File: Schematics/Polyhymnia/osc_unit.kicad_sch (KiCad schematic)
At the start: 7 parts, among them J4 Conn_02x05_Counter_Clockwise, SW10 RotaryEncoder, SW5 RotaryEncoder

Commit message: Added schematics for OSC, Filter and Envelope and updated README
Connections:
- no-connect marks 0 -> 1
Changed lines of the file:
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@@
 		(color 0 0 0 0)
 	)
+	(no_connect
+		(at 157.48 59.69)
+	)
 	(wire
 		(pts
@@
 		(pts
 			(xy 132.08 64.77) (xy 144.78 64.77)
+		)
+		(stroke
+			(width 0)
+			(type default)
+		)
+	)
+	(wire
+		(pts
+			(xy 5.4074 0.8096) (xy 5.4074 5.8896)
 		)
 		(stroke
@@
 			)
 			(justify left)
+		)
+	)
+	(hierarchical_label "GND"
+		(shape input)
+		(at 5.4074 0.8096 180)
+		(effects
+			(font
+				(size 1.27 1.27)
+			)
+			(justify right)
 		)
 	)
@@
 		(instances
 			(project "Polyhymnia"
-				(path "/e4936a91-9e28-4906-9468-02ad94b9239b/04017fce-ab7a-4c45-a3b8-5493e5fdc4a7"
+				(path "/e4936a91-9e28-4906-9468-02ad94b9239b/3627614c-7dfe-4a8f-9547-cf9b2f9e6ef0/0d039393-a65a-4236-aaaa-38dedb739ff5"
+					(reference "SW12")
+					(unit 1)
+				)
+				(path "/e4936a91-9e28-4906-9468-02ad94b9239b/3627614c-7dfe-4a8f-9547-cf9b2f9e6ef0/89248004-8614-47a4-bd14-f15ba37dba97"
+					(reference "SW14")
+					(unit 1)
+				)
+				(path "/e4936a91-9e28-4906-9468-02ad94b9239b/3627614c-7dfe-4a8f-9547-cf9b2f9e6ef0/a5d4020b-3f52-4bac-b91d-f4cfb91e59d1"
 					(reference "SW5")
-					(unit 1)
-				)
-				(path "/e4936a91-9e28-4906-9468-02ad94b9239b/4ef4e00a-50a0-4639-950e-6d0b1ade7b2c"
-					(reference "SW14")
-					(unit 1)
-				)
-				(path "/e4936a91-9e28-4906-9468-02ad94b9239b/acb5abcb-989c-4dca-8a1a-ed3e163b2d20"
-					(reference "SW12")
 					(unit 1)
 				)
@@
 		(instances
 			(project "Polyhymnia"
-				(path "/e4936a91-9e28-4906-9468-02ad94b9239b/04017fce-ab7a-4c45-a3b8-5493e5fdc4a7"
+				(path "/e4936a91-9e28-4906-9468-02ad94b9239b/3627614c-7dfe-4a8f-9547-cf9b2f9e6ef0/0d039393-a65a-4236-aaaa-38dedb739ff5"
+					(reference "D38")
+					(unit 1)
+				)
+				(path "/e4936a91-9e28-4906-9468-02ad94b9239b/3627614c-7dfe-4a8f-9547-cf9b2f9e6ef0/89248004-8614-47a4-bd14-f15ba37dba97"
+					(reference "D42")
+					(unit 1)
+				)
+				(path "/e4936a91-9e28-4906-9468-02ad94b9239b/3627614c-7dfe-4a8f-9547-cf9b2f9e6ef0/a5d4020b-3f52-4bac-b91d-f4cfb91e59d1"
 					(reference "D35")
-					(unit 1)
-				)
-				(path "/e4936a91-9e28-4906-9468-02ad94b9239b/4ef4e00a-50a0-4639-950e-6d0b1ade7b2c"
-					(reference "D42")
-					(unit 1)
-				)
-				(path "/e4936a91-9e28-4906-9468-02ad94b9239b/acb5abcb-989c-4dca-8a1a-ed3e163b2d20"
-					(reference "D38")
 					(unit 1)
 				)
@@
 		(instances
 			(project "Polyhymnia"
-				(path "/e4936a91-9e28-4906-9468-02ad94b9239b/04017fce-ab7a-4c45-a3b8-5493e5fdc4a7"
+				(path "/e4936a91-9e28-4906-9468-02ad94b9239b/3627614c-7dfe-4a8f-9547-cf9b2f9e6ef0/0d039393-a65a-4236-aaaa-38dedb739ff5"
+					(reference "SW11")
+					(unit 1)
+				)
+				(path "/e4936a91-9e28-4906-9468-02ad94b9239b/3627614c-7dfe-4a8f-9547-cf9b2f9e6ef0/89248004-8614-47a4-bd14-f15ba37dba97"
+					(reference "SW13")
+					(unit 1)
+				)
+				(path "/e4936a91-9e28-4906-9468-02ad94b9239b/3627614c-7dfe-4a8f-9547-cf9b2f9e6ef0/a5d4020b-3f52-4bac-b91d-f4cfb91e59d1"
 					(reference "SW10")
-					(unit 1)
-				)
-				(path "/e4936a91-9e28-4906-9468-02ad94b9239b/4ef4e00a-50a0-4639-950e-6d0b1ade7b2c"
-					(reference "SW13")
-					(unit 1)
-				)
-				(path "/e4936a91-9e28-4906-9468-02ad94b9239b/acb5abcb-989c-4dca-8a1a-ed3e163b2d20"
-					(reference "SW11")
 					(unit 1)
 				)
@@
 		(instances
 			(project "Polyhymnia"
-				(path "/e4936a91-9e28-4906-9468-02ad94b9239b/04017fce-ab7a-4c45-a3b8-5493e5fdc4a7"
+				(path "/e4936a91-9e28-4906-9468-02ad94b9239b/3627614c-7dfe-4a8f-9547-cf9b2f9e6ef0/0d039393-a65a-4236-aaaa-38dedb739ff5"
+					(reference "J5")
+					(unit 1)
+				)
+				(path "/e4936a91-9e28-4906-9468-02ad94b9239b/3627614c-7dfe-4a8f-9547-cf9b2f9e6ef0/89248004-8614-47a4-bd14-f15ba37dba97"
+					(reference "J6")
+					(unit 1)
+				)
+				(path "/e4936a91-9e28-4906-9468-02ad94b9239b/3627614c-7dfe-4a8f-9547-cf9b2f9e6ef0/a5d4020b-3f52-4bac-b91d-f4cfb91e59d1"
 					(reference "J4")
-					(unit 1)
-				)
-				(path "/e4936a91-9e28-4906-9468-02ad94b9239b/4ef4e00a-50a0-4639-950e-6d0b1ade7b2c"
-					(reference "J6")
-					(unit 1)
-				)
-				(path "/e4936a91-9e28-4906-9468-02ad94b9239b/acb5abcb-989c-4dca-8a1a-ed3e163b2d20"
-					(reference "J5")
 					(unit 1)
 				)
@@
 		(instances
 			(project "Polyhymnia"
-				(path "/e4936a91-9e28-4906-9468-02ad94b9239b/04017fce-ab7a-4c45-a3b8-5493e5fdc4a7"
+				(path "/e4936a91-9e28-4906-9468-02ad94b9239b/3627614c-7dfe-4a8f-9547-cf9b2f9e6ef0/0d039393-a65a-4236-aaaa-38dedb739ff5"
+					(reference "D41")
+					(unit 1)
+				)
+				(path "/e4936a91-9e28-4906-9468-02ad94b9239b/3627614c-7dfe-4a8f-9547-cf9b2f9e6ef0/89248004-8614-47a4-bd14-f15ba37dba97"
+					(reference "D45")
+					(unit 1)
+				)
+				(path "/e4936a91-9e28-4906-9468-02ad94b9239b/3627614c-7dfe-4a8f-9547-cf9b2f9e6ef0/a5d4020b-3f52-4bac-b91d-f4cfb91e59d1"
 					(reference "D34")
-					(unit 1)
-				)
-				(path "/e4936a91-9e28-4906-9468-02ad94b9239b/4ef4e00a-50a0-4639-950e-6d0b1ade7b2c"
-					(reference "D45")
-					(unit 1)
-				)
-				(path "/e4936a91-9e28-4906-9468-02ad94b9239b/acb5abcb-989c-4dca-8a1a-ed3e163b2d20"
-					(reference "D41")
 					(unit 1)
 				)
@@
 		(instances
 			(project "Polyhymnia"
-				(path "/e4936a91-9e28-4906-9468-02ad94b9239b/04017fce-ab7a-4c45-a3b8-5493e5fdc4a7"
+				(path "/e4936a91-9e28-4906-9468-02ad94b9239b/3627614c-7dfe-4a8f-9547-cf9b2f9e6ef0/0d039393-a65a-4236-aaaa-38dedb739ff5"
+					(reference "D39")
+					(unit 1)
+				)
+				(path "/e4936a91-9e28-4906-9468-02ad94b9239b/3627614c-7dfe-4a8f-9547-cf9b2f9e6ef0/89248004-8614-47a4-bd14-f15ba37dba97"
+					(reference "D43")
+					(unit 1)
+				)
+				(path "/e4936a91-9e28-4906-9468-02ad94b9239b/3627614c-7dfe-4a8f-9547-cf9b2f9e6ef0/a5d4020b-3f52-4bac-b91d-f4cfb91e59d1"
 					(reference "D37")
-					(unit 1)
-				)
-				(path "/e4936a91-9e28-4906-9468-02ad94b9239b/4ef4e00a-50a0-4639-950e-6d0b1ade7b2c"
-					(reference "D43")
-					(unit 1)
-				)
-				(path "/e4936a91-9e28-4906-9468-02ad94b9239b/acb5abcb-989c-4dca-8a1a-ed3e163b2d20"
-					(reference "D39")
 					(unit 1)
 				)
@@
 		(instances
 			(project "Polyhymnia"
-				(path "/e4936a91-9e28-4906-9468-02ad94b9239b/04017fce-ab7a-4c45-a3b8-5493e5fdc4a7"
+				(path "/e4936a91-9e28-4906-9468-02ad94b9239b/3627614c-7dfe-4a8f-9547-cf9b2f9e6ef0/0d039393-a65a-4236-aaaa-38dedb739ff5"
+					(reference "D40")
+					(unit 1)
+				)
+				(path "/e4936a91-9e28-4906-9468-02ad94b9239b/3627614c-7dfe-4a8f-9547-cf9b2f9e6ef0/89248004-8614-47a4-bd14-f15ba37dba97"
+					(reference "D44")
+					(unit 1)
+				)
+				(path "/e4936a91-9e28-4906-9468-02ad94b9239b/3627614c-7dfe-4a8f-9547-cf9b2f9e6ef0/a5d4020b-3f52-4bac-b91d-f4cfb91e59d1"
 					(reference "D36")
 					(unit 1)
 				)
-				(path "/e4936a91-9e28-4906-9468-02ad94b9239b/4ef4e00a-50a0-4639-950e-6d0b1ade7b2c"
-					(reference "D44")
-					(unit 1)
-				)
-				(path "/e4936a91-9e28-4906-9468-02ad94b9239b/acb5abcb-989c-4dca-8a1a-ed3e163b2d20"
-					(reference "D40")
-					(unit 1)
-				)

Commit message: Updated schematics
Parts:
- added R33, R36, R39, R42: 68 Ohm, symbol Device:R
- renumbered D35 to D34, D37 to D35, D34 to D37, SW10 to SW1, SW5 to SW2
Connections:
- net LED_SAW: now also R36.1; no longer J4.2 (Pin_2)
- net LED_SINE: now also R33.1; no longer J4.7 (Pin_7)
- net LED_SQUARE: now also R42.1; no longer J4.6 (Pin_6)
- net LED_TRIANGLE: now also R39.1; no longer J4.3 (Pin_3)
- new net: J4.2 (Pin_2), R36.2
- new net: J4.7 (Pin_7), R33.2
- new net: J4.3 (Pin_3), R39.2
- new net: J4.6 (Pin_6), R42.2
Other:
- note added: "Note to myself: 04 Frequency PhaseA PC0 05 Frequency PhaseB PC1 06 LED PC2 07 LED PC3 08 LED PC4 09 LED DEAD 10 A PC6 10 GND 11 B PC7"

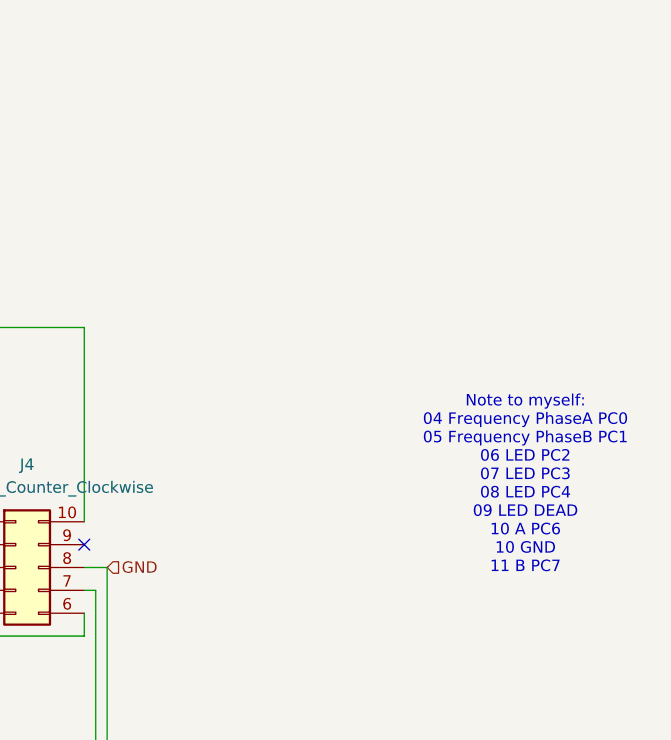
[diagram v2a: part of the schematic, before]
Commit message: Added audio amplifier schematics
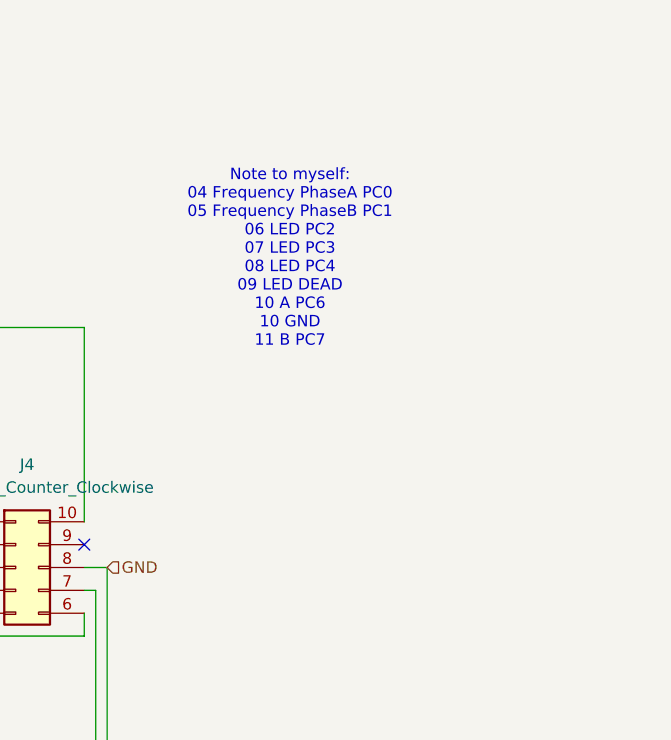
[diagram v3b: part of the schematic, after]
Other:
- title: (none) -> Oscillator Control Unit
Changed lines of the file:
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@@
 	(generator "eeschema")
 	(generator_version "10.0")
-	(paper "A4")
+	(paper "A5")
+	(title_block
+		(title "Oscillator Control Unit")
+		(date "2026-06-13")
+		(rev "0.2")
+	)
 	(text "Note to myself:\n04 Frequency PhaseA PC0\n05 Frequency PhaseB PC1\n06 LED PC2\n07 LED PC3\n08 LED PC4\n09 LED DEAD\n10 A PC6\n10 GND\n11 B PC7"
 		(exclude_from_sim no)
-		(at 206.502 53.086 0)
+		(at 180.34 27.94 0)
 		(effects
 			(font
